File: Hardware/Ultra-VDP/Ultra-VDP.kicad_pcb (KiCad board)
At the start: 4 copper layers, 60.9 x 29.7 mm, 74 parts, among them J1 BC075-05, J2 BC075-10, J3 CBUS, J4 BC075-10, J5 BC075-06, J6 BC075-10, J7 BC075-10, J8 BC075-05, U14 V53C8125HT30, U3 V9958, U6 LMH1980, Y1 21.477270MHz, Y3 4.433618MHz

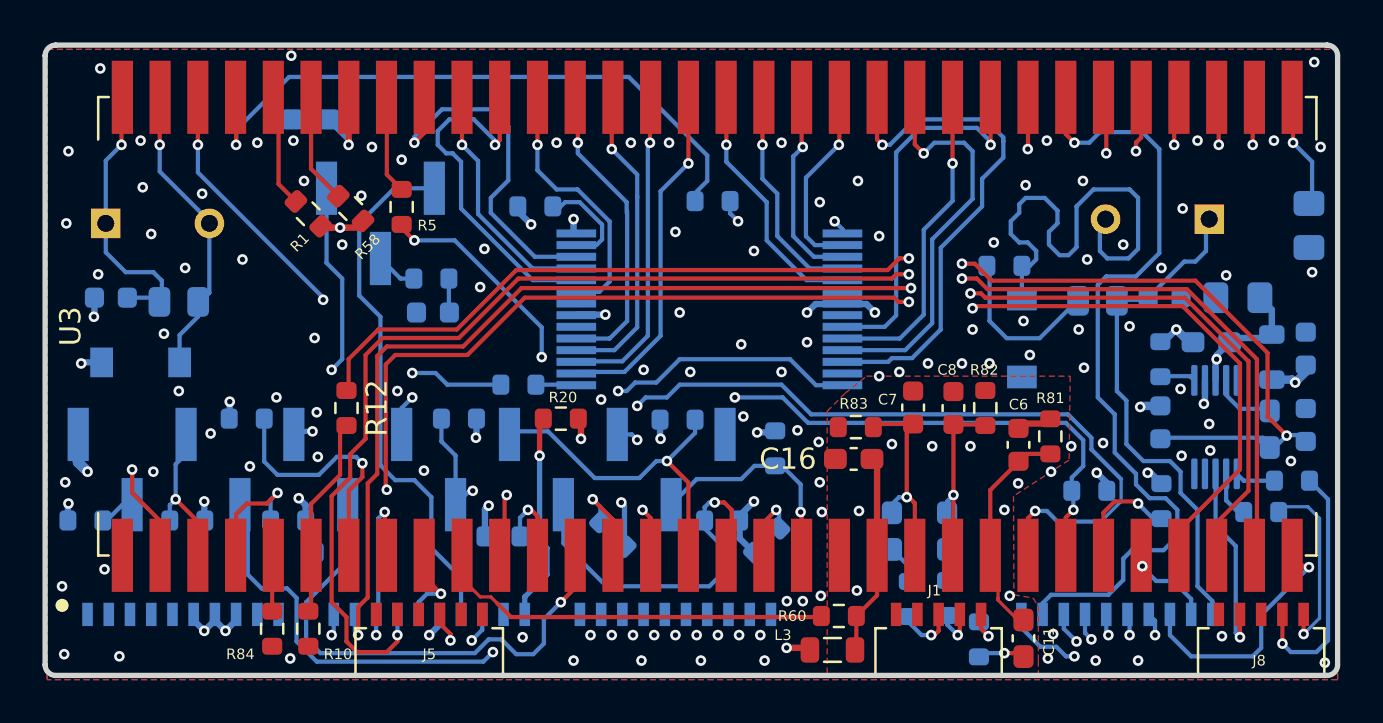
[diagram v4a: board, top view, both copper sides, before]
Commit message: Many tweaks and changes, such as a slight redesign of the VDP-baord.
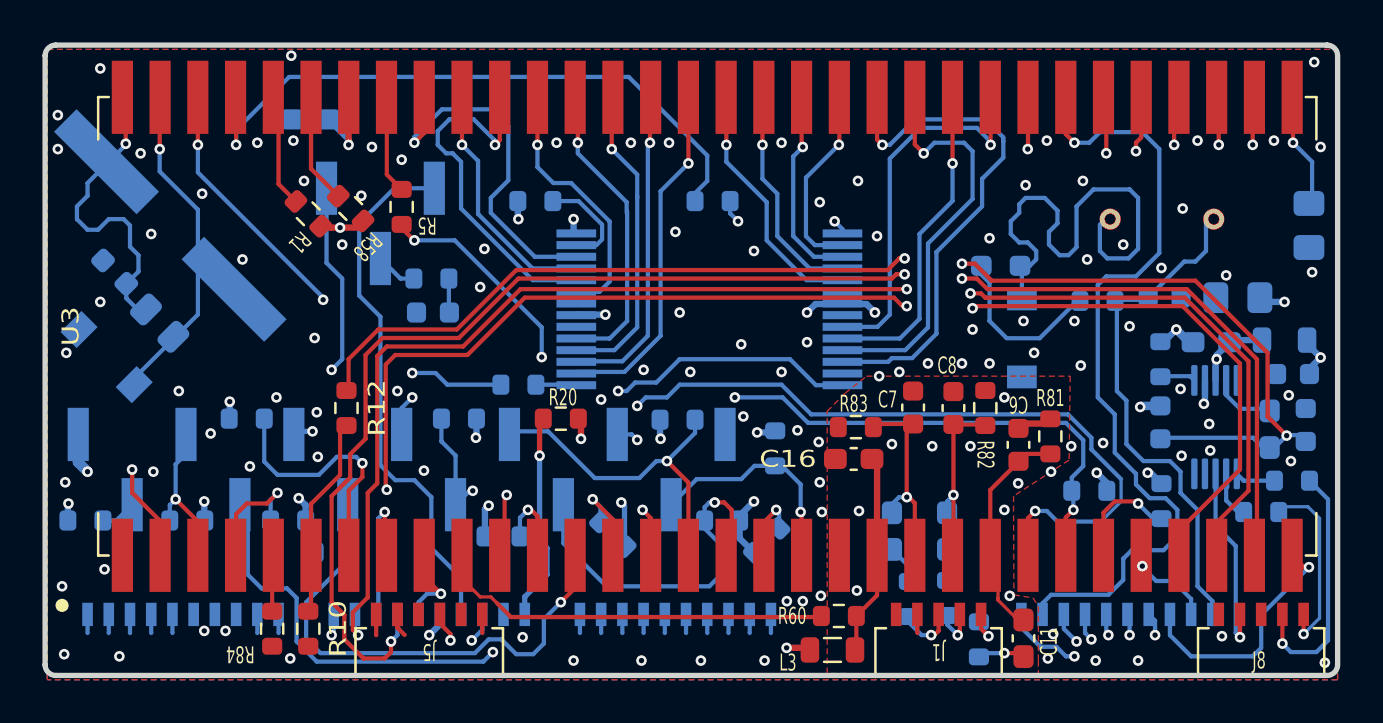
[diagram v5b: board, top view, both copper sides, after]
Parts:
- added trace1: pcb-trace, LRJ:NetTie-2_SMD_Pad0.2mm, F.Cu at (136.2, 115.1)
- added trace10: pcb-trace, LRJ:NetTie-2_SMD_Pad0.2mm, B.Cu at (125.3, 115.1)
- added trace11: pcb-trace, LRJ:NetTie-2_SMD_Pad0.2mm, B.Cu at (124.3, 115.1)
- added trace12: pcb-trace, LRJ:NetTie-2_SMD_Pad0.2mm, B.Cu at (123.3, 115.1)
- added trace13: pcb-trace, LRJ:NetTie-2_SMD_Pad0.2mm, B.Cu at (122.3, 115.1)
- added trace14: pcb-trace, LRJ:NetTie-2_SMD_Pad0.2mm, B.Cu at (121.3, 115.1)
- added trace15: pcb-trace, LRJ:NetTie-2_SMD_Pad0.2mm, B.Cu at (120.3, 115.1)
- added trace16: pcb-trace, LRJ:NetTie-2_SMD_Pad0.2mm, B.Cu at (106.1, 115.1)
- added trace17: pcb-trace, LRJ:NetTie-2_SMD_Pad0.2mm, B.Cu at (105.1, 115.1)
- added trace18: pcb-trace, LRJ:NetTie-2_SMD_Pad0.2mm, B.Cu at (101.1, 115.1)
- added trace19: pcb-trace, LRJ:NetTie-2_SMD_Pad0.2mm, B.Cu at (100.1, 115.1)
- added trace2: pcb-trace, LRJ:NetTie-2_SMD_Pad0.2mm, F.Cu at (110.7, 115.2)
- added trace20: pcb-trace, LRJ:NetTie-2_SMD_Pad0.2mm, B.Cu at (99.1, 115.1)
- added trace21: pcb-trace, LRJ:NetTie-2_SMD_Pad0.2mm, B.Cu at (98.1, 115.1)
- added trace22: pcb-trace, LRJ:NetTie-2_SMD_Pad0.2mm, B.Cu at (97.1, 115.1)
- added trace3: pcb-trace, LRJ:NetTie-2_SMD_Pad0.2mm, F.Cu at (111.9, 115.2)
- added trace4: pcb-trace, LRJ:NetTie-2_SMD_Pad0.2mm, F.Cu at (115.7, 115.1)
- added trace6: pcb-trace, LRJ:NetTie-2_SMD_Pad0.2mm, B.Cu at (129.3, 115.1)
- added trace7: pcb-trace, LRJ:NetTie-2_SMD_Pad0.2mm, B.Cu at (128.3, 115.1)
- added trace8: pcb-trace, LRJ:NetTie-2_SMD_Pad0.2mm, B.Cu at (127.3, 115.1)
- added trace9: pcb-trace, LRJ:NetTie-2_SMD_Pad0.2mm, B.Cu at (126.3, 115.1)
- C12, C19: value 47pF -> C_CC0603JRNPO9BN470
- R10, R13, R14, R15: value 75 -> R_ERJ-PA3F75R0V; footprint Resistor_SMD:R_0603_1608Metric -> LRJ:R_0603_1608Metric_roundcourt
- R12, R27, R5, R6, R61, R8: value 100 -> R_CRGP0603F220R
- R3: value 1k -> R_ERA-3VRW1001V; footprint Resistor_SMD:R_0603_1608Metric -> Resistor_SMD:R_0603_1608Metric_Pad0.98x0.95mm_HandSolder
- R4: value 1M -> R_ERJ-3GEYJ105V; footprint Resistor_SMD:R_0805_2012Metric -> Resistor_SMD:R_0603_1608Metric
- Y1: value 21.477270MHz -> Y_HCM4921477270ABJT; footprint Ultra-MSX:Crystal_HC-49U_Vert -> LRJ:Crystal_HC49-US_Vertical_SMD
- Y3: value 4.433618MHz -> Y_ECS-44-20-4X; footprint Ultra-MSX:Crystal_HC-49U_Vert -> LRJ:Crystal_HC49-US_Vertical_THT
- moved Y1 3.04 mm to (101.0, 96.1), turned to -45 degrees
- moved Y3 2.22 mm to (147.7, 95.8)
- moved C1 1.62 mm to (98.0, 102.3), turned to -45 degrees
- moved R2 1.35 mm to (100.5, 100.7), turned to -45 degrees
- moved C18 1.34 mm to (153.9, 103.1), turned to 180 degrees
- moved C2 1.22 mm to (98.4, 98.3), turned to -45 degrees
- moved L1 1.00 mm to (153.5, 101.5), turned to 180 degrees
- moved R7 0.25 mm to (118.2, 95.0)
- moved R3 0.18 mm to (140.1, 98.0), turned to 0 degrees
- turned R10 to 90 degrees
- turned R13 to -90 degrees
- turned R14 to -90 degrees
- turned R15 to 90 degrees
- turned R4 to 180 degrees
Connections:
- C16 pad 1: GNDA -> GND
- C17 pad 1: /+5V_SYNC -> VDDSYNC
- C6 pad 2: GNDA -> GND
- C7 pad 2: GNDA -> GND
- C73 pad 1: /+5V_SYNC -> +5V
- C8 pad 2: GNDA -> GND
- J1 pad 1: GNDA -> GND
- J1 pad 3: /G-Main -> /G-Mb
- J1 pad 4: /R-Main -> /R-Mb
- J1 pad 5: /B-Main -> /B-Mb
- L1 pad 2: /+5V_SYNC -> VDDSYNC
- R10 pad 1: /COMPSYNC -> GND
- R10 pad 2: GND -> /COMPSYNC
- R13 pad 1: /R-Main -> /RED2
- R13 pad 2: /RED2 -> /R-Mb
- R14 pad 1: /G-Main -> /GREEN2
- R14 pad 2: /GREEN2 -> /G-Mb
- R15 pad 1: /B-Main -> /BLUE2
- R15 pad 2: /BLUE2 -> /B-Mb
- R3 pad 1: /PAL_CLK_IN- -> Net-(R3-Pad1)
- R3 pad 2: Net-(R3-Pad2) -> /PAL_CLK_IN-
- R4 pad 1: Net-(R3-Pad2) -> /PAL_CLK_IN+
- R4 pad 2: /PAL_CLK_IN+ -> Net-(R3-Pad1)
- R81 pad 2: GNDA -> GND
- R82 pad 2: GNDA -> GND
- R83 pad 2: GNDA -> GND
- U3 pad 20: GNDA -> GND
- U6 pad 3: /+5V_SYNC -> VDDSYNC
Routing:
- net Net-(R3-Pad1): track 0.00 -> 8.03 mm
- net Net-(R3-Pad2): track 7.91 -> 0.00 mm
- net /+5V_SYNC: track 6.18 -> 0.00 mm, vias 1 -> 0
- net GND: track 15.5 -> 11.2 mm, vias 100 -> 103
- net VDDSYNC: track 0.00 -> 3.64 mm, vias 0 -> 1
- net /G-Mb: track 0.00 -> 2.77 mm, vias 0 -> 1
- net /G-Main: track 2.77 -> 0.00 mm, vias 1 -> 0
- net /R-Mb: track 0.00 -> 2.15 mm, vias 0 -> 1
- net /R-Main: track 2.15 -> 0.00 mm, vias 1 -> 0
- net /B-Mb: track 0.00 -> 2.03 mm, vias 0 -> 1
- net /B-Main: track 2.03 -> 0.00 mm, vias 1 -> 0
- net /XTAL-: track 13.1 -> 14.8 mm
- net GNDA: track 1.37 -> 0.00 mm, vias 5 -> 0
- net +5V: track 31.4 -> 32.6 mm, vias 21 -> 22
- net /XTAL1+: track 14.1 -> 15.4 mm
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- removed copper zone on F.Cu, net GNDA
- removed copper zone on In1.Cu, net GNDA
